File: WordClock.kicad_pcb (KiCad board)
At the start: 2 copper layers, 100 x 100 mm, 91 parts, among them J1 Conn_01x01, J2 Conn_01x01, J3 Conn_01x01, J4 Conn_01x09, J5 Conn_01x08, J6 Conn_01x08, J7 Conn_01x08, SW1 SW_Push, SW2 SW_Push, SW3 SW_Push, SW4 SW_Push, SW5 SW_Push, U10 NUD3124, U12 NUD3124, U13 NUD3124, U14 NUD3124, U15 NUD3124, U16 NUD3124, U17 NUD3124, U18 NUD3124, U19 NUD3124, U20 NUD3124, U21 NUD3124, U22 NUD3124, U23 NUD3124, U3 ARDUINO_NANO, U4 MCP7940N, U5 MCP23017, U6 MCP23017, U7 NUD3124, U8 NUD3124, U9 NUD3124, Y1 Crystal

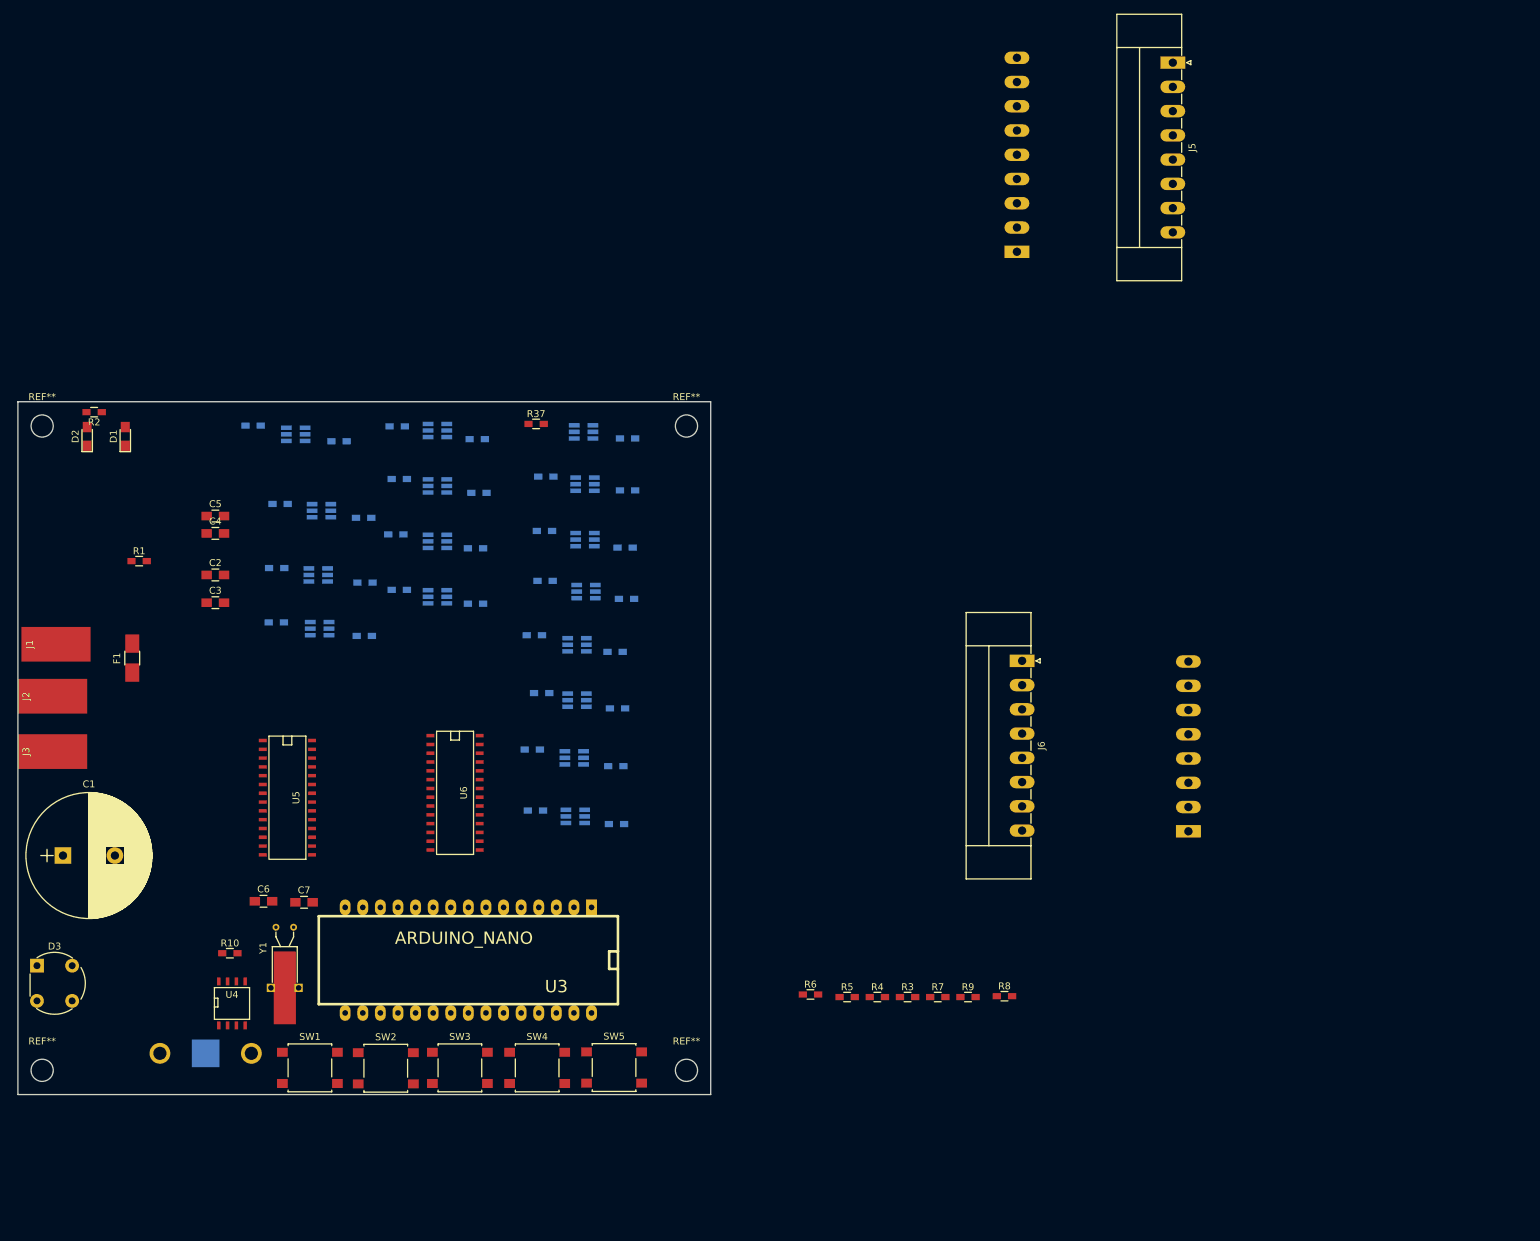
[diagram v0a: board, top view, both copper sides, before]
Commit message: Routed power, clock, switches and started on arduino/IO expanders
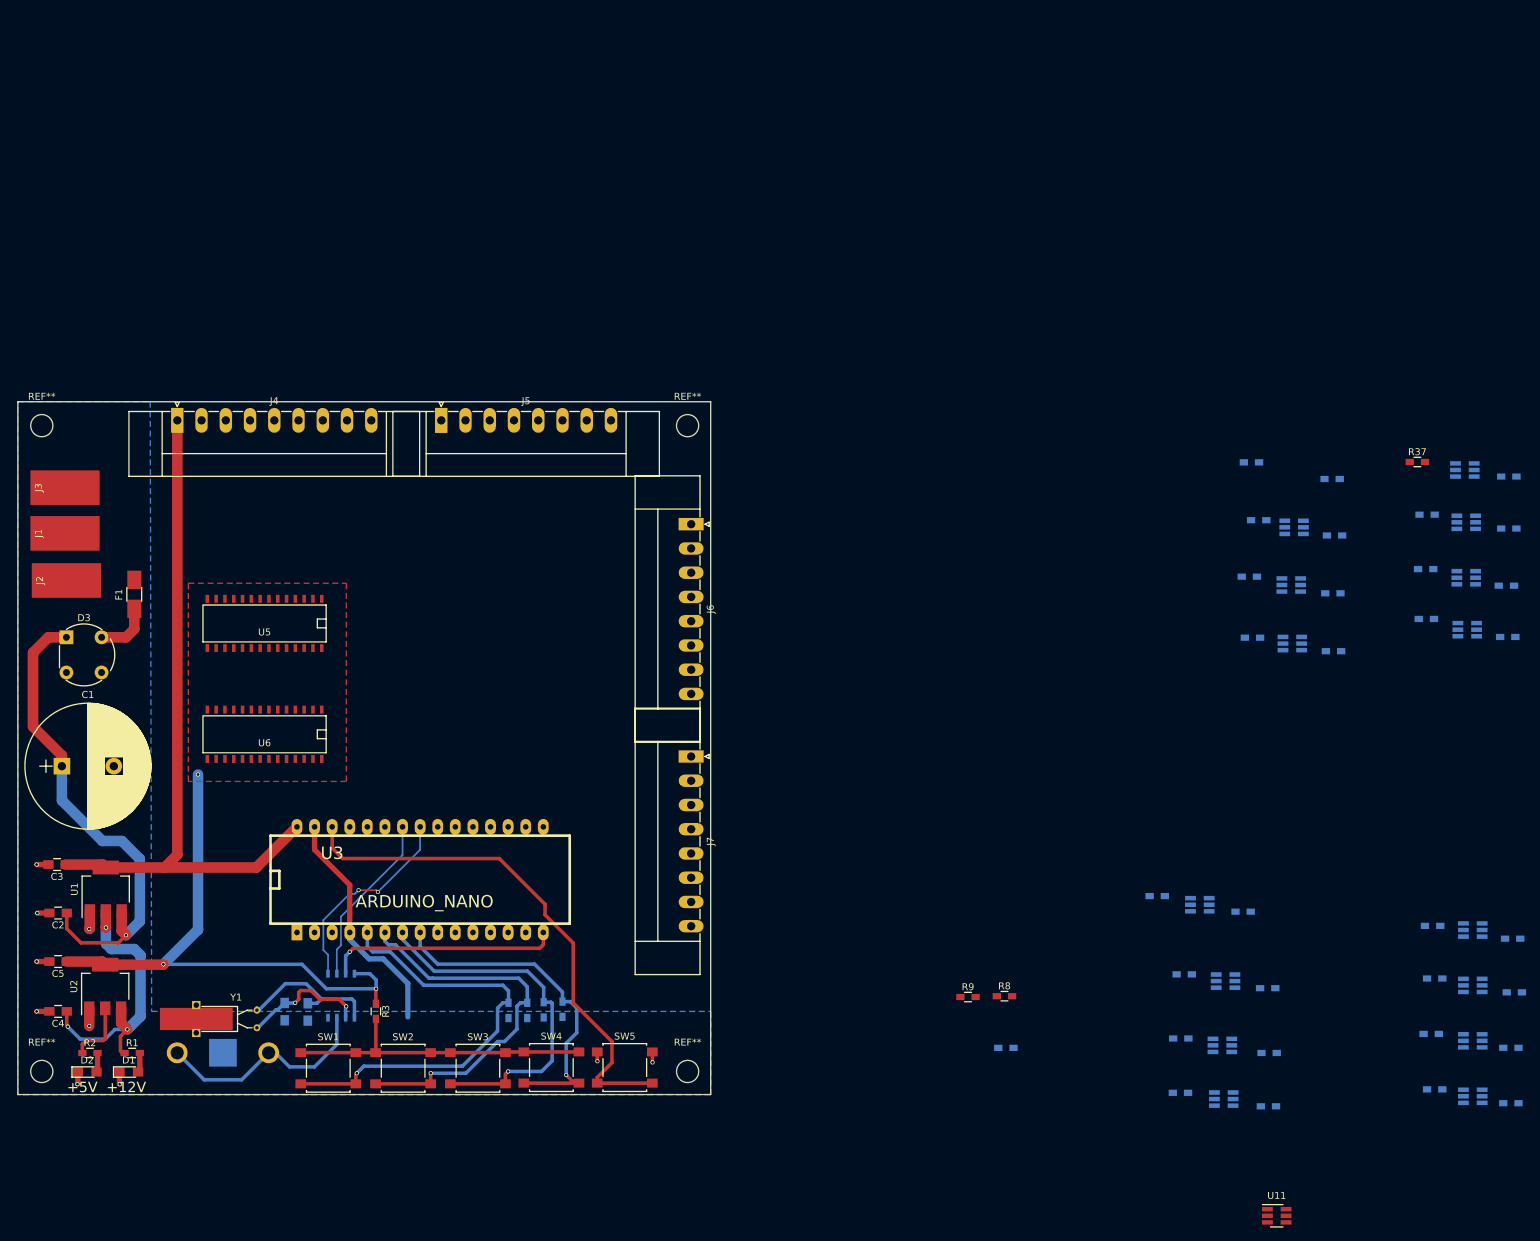
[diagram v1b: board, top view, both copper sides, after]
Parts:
- removed the REF** at (28.5, 28.5)
- removed the REF** at (121.5, 28.5)
- removed the REF** at (121.5, 121.5)
- removed the REF** at (28.5, 121.5)
- removed U23: NUD3124, TO_SOT_Packages_SMD:SOT-23-6_Handsoldering
- added REF**: MountingHole_3.2mm_M3, Mounting_Holes:MountingHole_3.2mm_M3, F.Cu at (28.4, 121.7)
- added REF**: MountingHole_3.2mm_M3, Mounting_Holes:MountingHole_3.2mm_M3, F.Cu at (121.7, 121.7)
- added REF**: MountingHole_3.2mm_M3, Mounting_Holes:MountingHole_3.2mm_M3, F.Cu at (121.7, 28.4)
- added REF**: MountingHole_3.2mm_M3, Mounting_Holes:MountingHole_3.2mm_M3, F.Cu at (28.4, 28.4)
- added U1: AP1117-50, TO_SOT_Packages_SMD:SOT-223-3_TabPin2, F.Cu at (37.7, 95.4)
- added U11: NUD3124, TO_SOT_Packages_SMD:SOT-23-6_Handsoldering, F.Cu at (206.7, 142.5)
- added U2: AP1117-50, TO_SOT_Packages_SMD:SOT-223-3_TabPin2, F.Cu at (37.6, 109.4)
- C2: value 33uF -> 10uF
- C3: value 0.1uF -> 10uF
- C4: value 33uF -> 4.7uF
- C5: value 0.1uF -> 4.7uF
- C6, C7, R10, R4, R5, R6, R7, U4: moved to B.Cu
- J4, J7: moved to F.Cu
- moved R11 165.9 mm to (229.5, 124.2)
- moved R15 165.9 mm to (240.5, 126.2)
- moved R19 165.9 mm to (229.0, 116.2)
- moved R23 165.9 mm to (240.5, 118.2)
- moved R27 165.9 mm to (229.5, 108.2)
- moved R31 165.9 mm to (241.0, 110.2)
- moved R35 165.9 mm to (229.2, 100.7)
- moved R39 165.9 mm to (240.8, 102.5)
- moved U12 165.9 mm to (235.0, 117.2)
- moved U16 165.9 mm to (235.0, 109.2)
- moved U20 165.9 mm to (235.0, 101.2)
- moved U7 165.9 mm to (235.0, 125.2)
- moved R12 147.1 mm to (192.8, 124.8)
- moved R16 147.1 mm to (205.5, 126.7)
- moved R20 147.1 mm to (192.8, 116.9)
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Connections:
- D3 pad 2: AC+ -> AC-
- J2 pad 1: AC+ -> AC-
- U12 pad 2: OUT3 -> OUT19
- U12 pad 3: Net-(R19-Pad1) -> Net-(R20-Pad1)
- U12 pad 5: OUT4 -> OUT20
- U12 pad 6: Net-(R23-Pad2) -> Net-(R24-Pad2)
- U13 pad 2: OUT19 -> OUT11
- U13 pad 3: Net-(R20-Pad1) -> Net-(R21-Pad1)
- U13 pad 5: OUT20 -> OUT12
- U13 pad 6: Net-(R24-Pad2) -> Net-(R25-Pad2)
- U14 pad 2: OUT11 -> OUT27
- U14 pad 3: Net-(R21-Pad1) -> Net-(R22-Pad1)
- U14 pad 5: OUT12 -> OUT28
- U14 pad 6: Net-(R25-Pad2) -> Net-(R26-Pad2)
- U15 pad 2: OUT27 -> OUT5
- U15 pad 3: Net-(R22-Pad1) -> Net-(R27-Pad1)
- U15 pad 5: OUT28 -> OUT6
- U15 pad 6: Net-(R26-Pad2) -> Net-(R31-Pad2)
- U16 pad 2: OUT5 -> OUT21
- U16 pad 3: Net-(R27-Pad1) -> Net-(R28-Pad1)
- U16 pad 5: OUT6 -> OUT22
- U16 pad 6: Net-(R31-Pad2) -> Net-(R32-Pad2)
- U17 pad 2: OUT21 -> OUT13
- U17 pad 3: Net-(R28-Pad1) -> Net-(R29-Pad1)
- U17 pad 5: OUT22 -> OUT14
- U17 pad 6: Net-(R32-Pad2) -> Net-(R33-Pad2)
- U18 pad 2: OUT13 -> OUT29
- U18 pad 3: Net-(R29-Pad1) -> Net-(R30-Pad1)
- U18 pad 5: OUT14 -> OUT30
- U18 pad 6: Net-(R33-Pad2) -> Net-(R34-Pad2)
- U19 pad 2: OUT29 -> OUT7
- U19 pad 3: Net-(R30-Pad1) -> Net-(R35-Pad1)
- U19 pad 5: OUT30 -> OUT8
- U19 pad 6: Net-(R34-Pad2) -> Net-(R39-Pad2)
- U20 pad 2: OUT7 -> OUT23
- U20 pad 3: Net-(R35-Pad1) -> Net-(R36-Pad1)
- U20 pad 5: OUT8 -> OUT24
- U20 pad 6: Net-(R39-Pad2) -> Net-(R40-Pad2)
- U21 pad 2: OUT23 -> OUT15
- U21 pad 3: Net-(R36-Pad1) -> Net-(R37-Pad1)
- U21 pad 5: OUT24 -> OUT16
- U21 pad 6: Net-(R40-Pad2) -> Net-(R41-Pad2)
- U22 pad 2: OUT15 -> OUT31
- U22 pad 3: Net-(R37-Pad1) -> Net-(R38-Pad1)
- U22 pad 5: OUT16 -> OUT32
- U22 pad 6: Net-(R41-Pad2) -> Net-(R42-Pad2)
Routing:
- net +12V: track 0.00 -> 143.0 mm, vias 0 -> 3
- net +5V: track 0.00 -> 92.0 mm, vias 0 -> 3
- net Net-(SW5-Pad2): track 0.00 -> 75.8 mm
- net Net-(C1-Pad1): track 0.00 -> 71.2 mm, vias 0 -> 1
- net Net-(R4-Pad1): track 0.00 -> 64.4 mm, vias 0 -> 1
- net Net-(R5-Pad1): track 0.00 -> 56.4 mm, vias 0 -> 1
- net GND: track 0.00 -> 52.9 mm, vias 0 -> 10
- net Net-(R6-Pad1): track 0.00 -> 52.9 mm, vias 0 -> 1
- net Net-(R7-Pad1): track 0.00 -> 49.7 mm, vias 0 -> 1
- net Net-(R3-Pad2): track 0.00 -> 45.1 mm
- net MFP: track 0.00 -> 33.5 mm, vias 0 -> 1
- net Net-(BT1-Pad1): track 0.00 -> 33.3 mm
- net SDA: track 0.00 -> 29.7 mm, vias 0 -> 2
- net SCL: track 0.00 -> 25.1 mm
- net Net-(C6-Pad2): track 0.00 -> 21.6 mm
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- added copper zone on F.Cu, net +5V
- added copper zone on B.Cu, net GND
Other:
- board text added: "+12V"
- board text added: "+5V"

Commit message: Continued with routing and board layout.
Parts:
- R11, R12, R13, R14, R15, R16, R17, R18, R19, R20, R21, R22, R23, R24, R25, R26, R27, R28, R29, R30, R31, R32, R33, R34, R35, R36, R38, R39, R40, R41, R42, U10, U13, U14, U15, U16, U17, U18, U19, U20, U21, U22, U7, U9: moved to F.Cu
- U3: footprint arduino:arduino_mini -> Modules:Arduino_Nano
- moved R15 204.5 mm to (55.0, 40.2), turned to 270 degrees
- moved U7 198.3 mm to (53.2, 46.0)
- moved R11 196.9 mm to (51.4, 40.2), turned to 90 degrees
- moved R23 194.8 mm to (62.0, 40.2), turned to 270 degrees
- moved R19 186.6 mm to (58.6, 40.2), turned to 90 degrees
- moved R31 185.7 mm to (69.0, 40.2), turned to 270 degrees
- moved R27 177.5 mm to (65.6, 40.2), turned to 90 degrees
- moved R39 176.1 mm to (76.0, 40.2), turned to 270 degrees
- moved U11 175.3 mm to (60.4, 46.0)
- moved R35 168.0 mm to (72.4, 40.2), turned to 90 degrees
- moved R17 151.5 mm to (89.7, 40.3), turned to 270 degrees
- moved U22 150.7 mm to (103.0, 109.6), turned to 180 degrees
- moved U9 147.0 mm to (87.7, 46.0)
- moved U18 144.3 mm to (102.9, 102.5), turned to 180 degrees
- moved R25 143.7 mm to (96.6, 40.3), turned to 270 degrees
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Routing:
- net Net-(SW5-Pad2): track 75.8 -> 0.00 mm
- net OUT1: track 0.00 -> 42.1 mm, vias 0 -> 6
- net OUT15: track 0.00 -> 38.0 mm, vias 0 -> 2
- net OUT16: track 0.00 -> 37.6 mm, vias 0 -> 2
- net OUT2: track 0.00 -> 37.1 mm, vias 0 -> 4
- net OUT3: track 0.00 -> 37.1 mm, vias 0 -> 4
- net OUT14: track 0.00 -> 36.6 mm, vias 0 -> 2
- net MFP: track 33.5 -> 0.00 mm, vias 1 -> 0
- net OUT13: track 0.00 -> 33.1 mm, vias 0 -> 2
- net OUT12: track 0.00 -> 33.0 mm, vias 0 -> 2
- net OUT5: track 0.00 -> 32.7 mm, vias 0 -> 2
- net OUT4: track 0.00 -> 32.5 mm, vias 0 -> 2
- net SDA: track 29.7 -> 0.00 mm, vias 2 -> 0
- net OUT8: track 0.00 -> 29.1 mm, vias 0 -> 2
- net OUT9: track 0.00 -> 28.5 mm, vias 0 -> 2
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- removed copper zone on F.Cu, net +5V

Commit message: Finished routing board.
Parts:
- R10, R4, R5, R6, R7, U12, U8: moved to F.Cu
- moved R8 76.7 mm to (72.7, 109.8)
- moved R10 58.4 mm to (88.5, 95.1)
- moved R9 52.3 mm to (88.5, 98.0), turned to 180 degrees
- moved R4 15.4 mm to (110.3, 118.1), turned to 0 degrees
- moved R5 13.7 mm to (110.3, 119.9), turned to 0 degrees
- moved R6 13.0 mm to (110.3, 121.7), turned to 0 degrees
- moved R7 12.6 mm to (110.3, 123.4), turned to 0 degrees
- moved U8 7.22 mm to (94.8, 55.5), turned to 180 degrees
- moved U12 0.30 mm to (103.0, 64.0), turned to 180 degrees
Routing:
- net SDA: track 0.00 -> 127.4 mm, vias 0 -> 5
- net +5V: track 70.7 -> 196.5 mm, vias 2 -> 3
- net SCL: track 0.00 -> 123.7 mm, vias 0 -> 3
- net GND: track 52.8 -> 131.3 mm, vias 29 -> 53
- net OUT25: track 0.00 -> 64.6 mm, vias 0 -> 2
- net OUT27: track 0.00 -> 64.6 mm, vias 0 -> 2
- net OUT29: track 0.00 -> 60.8 mm, vias 0 -> 2
- net OUT31: track 0.00 -> 58.3 mm, vias 0 -> 2
- net OUT26: track 0.00 -> 55.3 mm, vias 0 -> 2
- net Net-(SW5-Pad2): track 0.00 -> 55.0 mm, vias 0 -> 4
- net Net-(R7-Pad1): track 23.0 -> 77.5 mm, vias 1 -> 5
- net OUT28: track 0.00 -> 53.6 mm, vias 0 -> 2
- net MFP: track 0.00 -> 53.1 mm, vias 0 -> 2
- net Net-(R6-Pad1): track 26.5 -> 77.9 mm, vias 1 -> 4
- net Net-(R4-Pad1): track 37.6 -> 88.3 mm, vias 1 -> 2
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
